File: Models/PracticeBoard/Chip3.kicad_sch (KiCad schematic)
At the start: 17 parts, among them U1 XMC1100

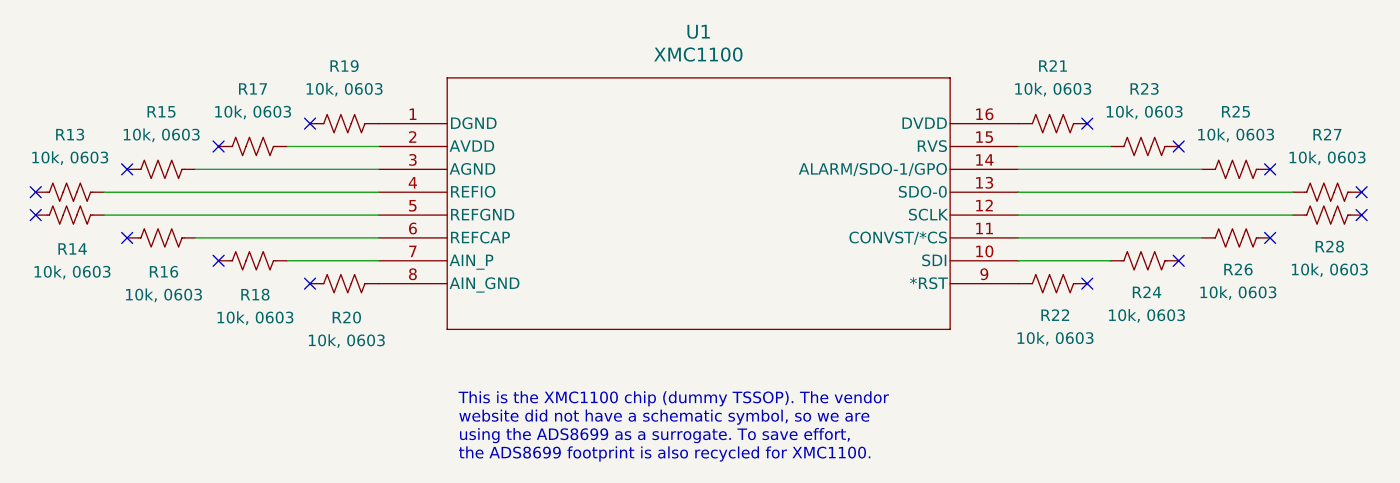
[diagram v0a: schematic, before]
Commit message: Finished the schematic for the practice board
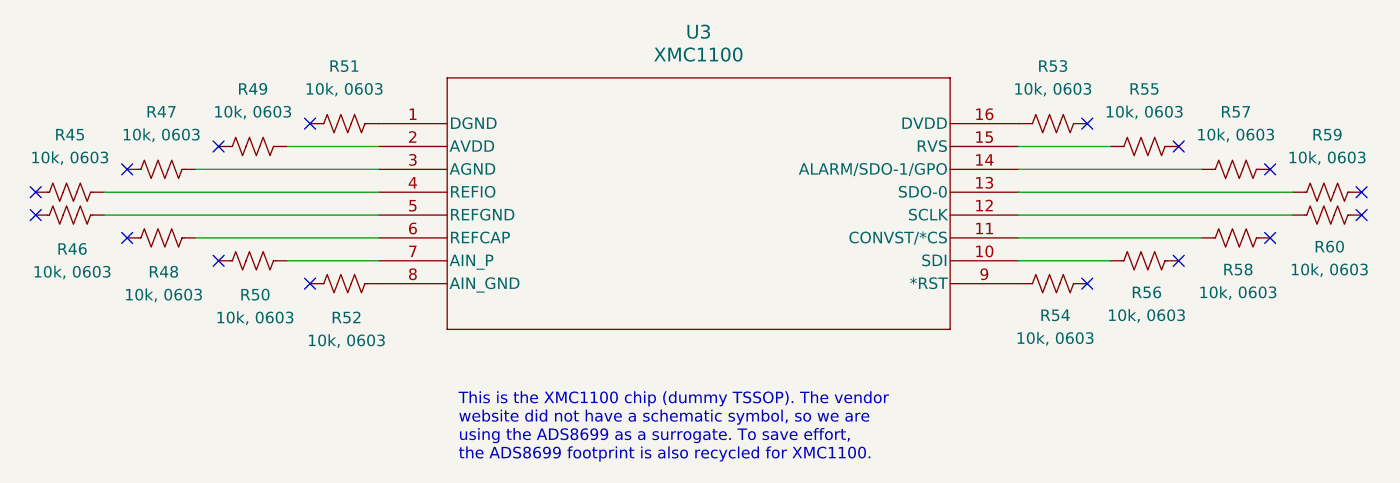
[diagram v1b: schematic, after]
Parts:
- removed R13, R14, R15, R16, R17, R18, R19, R20, R21, R22, R23, R24, R25, R26, R27, R28: 10k, 0603, TwoTerminal:RESC0603, symbol Device:R_US
- removed U1: XMC1100, IC:ADS8699, symbol ADS8699:ADS8699IPW
- added R45, R46, R47, R48, R49, R50, R51, R52, R53, R54, R55, R56, R57, R58, R59, R60: 10k, 0603, TwoTerminal:RESC0603, symbol Device:R_US
- added U3: XMC1100, IC:ADS8699, symbol ADS8699:ADS8699IPW
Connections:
- new net: R57.1, U3.14 (ALARM/SDO-1/GPO)
- new net: R54.1, U3.9 (*RST)
- new net: R52.2, U3.8 (AIN_GND)
- new net: R51.2, U3.1 (DGND)
- new net: R56.1, U3.10 (SDI)
- new net: R58.1, U3.11 (CONVST/*CS)
- new net: R60.1, U3.12 (SCLK)
- new net: R59.1, U3.13 (SDO-0)
- new net: R55.1, U3.15 (RVS)
- new net: R53.1, U3.16 (DVDD)
- new net: R49.2, U3.2 (AVDD)
- new net: R47.2, U3.3 (AGND)
- new net: R45.2, U3.4 (REFIO)
- new net: R46.2, U3.5 (REFGND)
- new net: R48.2, U3.6 (REFCAP)
- new net: R50.2, U3.7 (AIN_P)
